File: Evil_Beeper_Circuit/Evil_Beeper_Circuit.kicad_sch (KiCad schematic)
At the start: 0 parts

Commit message: added attiny to schematic
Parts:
- added U1: ATtiny85-20P, Package_DIP:DIP-8_W7.62mm, symbol MCU_Microchip_ATtiny:ATtiny85-20P
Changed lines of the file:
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@@
 	(generator_version "9.0")
 	(paper "A4")
+	(symbol
+		(lib_id "MCU_Microchip_ATtiny:ATtiny85-20P")
+		(at 88.9 91.44 0)
+		(unit 1)
+		(exclude_from_sim no)
+		(in_bom yes)
+		(on_board yes)
+		(dnp no)
+		(fields_autoplaced yes)
+		(property "Reference" "U1"
+			(at 74.93 90.1699 0)
+			(effects
+				(font
+					(size 1.27 1.27)
+				)
+				(justify right)
+			)
+		)
+		(property "Value" "ATtiny85-20P"
+			(at 74.93 92.7099 0)
+			(effects
+				(font
+					(size 1.27 1.27)
+				)
+				(justify right)
+			)
+		)
+		(property "Footprint" "Package_DIP:DIP-8_W7.62mm"
+			(at 88.9 91.44 0)
+			(effects
+				(font
+					(size 1.27 1.27)
+					(italic yes)
+				)
+				(hide yes)
+			)
+		)
+		(property "Datasheet" "http://ww1.microchip.com/downloads/en/DeviceDoc/atmel-2586-avr-8-bit-microcontroller-attiny25-attiny45-attiny85_datasheet.pdf"
+			(at 88.9 91.44 0)
+			(effects
+				(font
+					(size 1.27 1.27)
+				)
+				(hide yes)
+			)
+		)
+		(property "Description" "20MHz, 8kB Flash, 512B SRAM, 512B EEPROM, debugWIRE, DIP-8"
+			(at 88.9 91.44 0)
+			(effects
+				(font
+					(size 1.27 1.27)
+				)
+				(hide yes)
+			)
+		)
+		(pin "2"
+		)
+		(pin "4"
+		)
+		(pin "5"
+		)
+		(pin "1"
+		)
+		(pin "7"
+		)
+		(pin "6"
+		)
+		(pin "8"
+		)
+		(pin "3"
+		)
+		(instances
+			(project ""
+				(path "/7878dd5e-8ba5-4c58-8533-098f12b6f08b"
+					(reference "U1")
+					(unit 1)
+				)
+			)
+		)
+	)
 	(sheet_instances
 		(path "/"

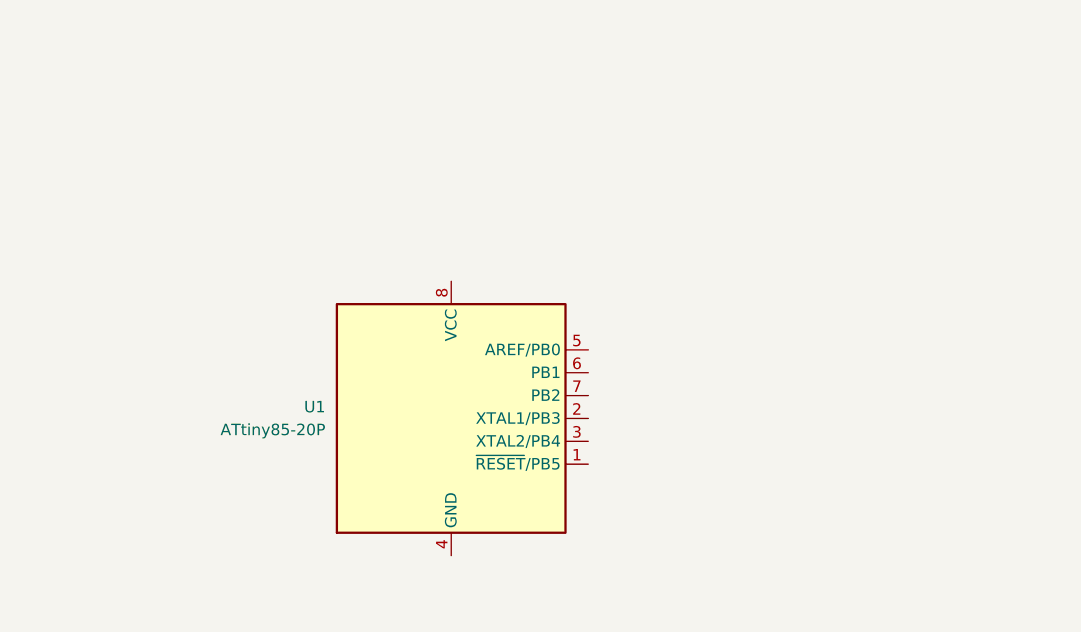
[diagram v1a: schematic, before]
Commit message: added circuit components
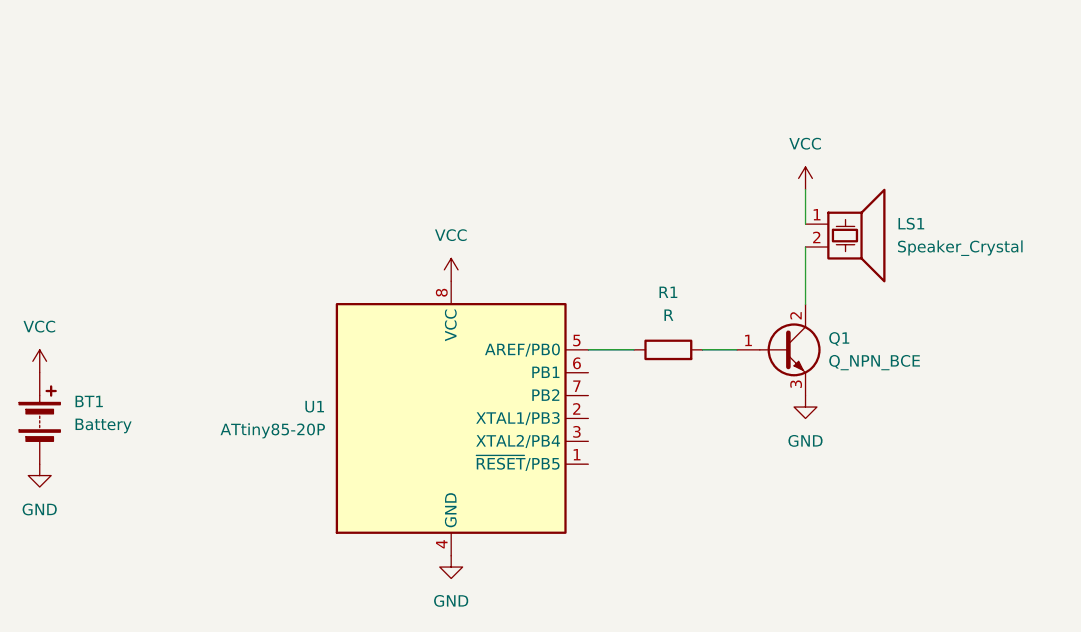
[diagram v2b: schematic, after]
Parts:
- added BT1: Battery, symbol Device:Battery
- added LS1: Speaker_Crystal, symbol Device:Speaker_Crystal
- added Q1: Q_NPN_BCE, symbol Transistor_BJT:Q_NPN_BCE
- added R1: R, symbol Device:R
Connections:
- net GND: now reaches U1.4 (GND)
- net GND: now also BT1.2 (-), Q1.3 (E)
- net at U1.5 (AREF/PB0): now also R1.1
- net VCC: now reaches U1.8 (VCC)
- net VCC: now also BT1.1 (+), LS1.1
- new net: LS1.2, Q1.2 (C)
- new net: Q1.1 (B), R1.2

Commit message: Designed PCB
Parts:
- removed Q1: Q_NPN_BCE, symbol Transistor_BJT:Q_NPN_BCE
- added C1: 22uF, Capacitor_THT:CP_Radial_D4.0mm_P1.50mm, symbol Device:C
- added C2: 100nF, Capacitor_THT:C_Rect_L7.2mm_W3.0mm_P5.00mm_FKS2_FKP2_MKS2_MKP2, symbol Device:C
- added Q1: Q_NPN_CBE, Package_TO_SOT_THT:TO-92_Inline, symbol Transistor_BJT:Q_NPN_CBE
- BT1: footprint (none) -> footprints:2032 Battery Holder
- LS1: footprint (none) -> footprints:Buzzer
- R1: value R -> 1k; footprint (none) -> Resistor_THT:R_Axial_DIN0207_L6.3mm_D2.5mm_P7.62mm_Horizontal
- U1: footprint Package_DIP:DIP-8_W7.62mm -> Package_DIP:DIP-8_W7.62mm_Socket
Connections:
- net GND: now also C1.1, C2.1, Q1.3 (E)
- net VCC: now also C1.2, C2.2
- net at LS1.2: now also Q1.1 (C)
- net at R1.2: now also Q1.2 (B)
